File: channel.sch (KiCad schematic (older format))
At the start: 8 parts, among them Q1 MMBT5551, Q2 MMBT5401, Q3 NTMS4807, Q4 NTMS4807

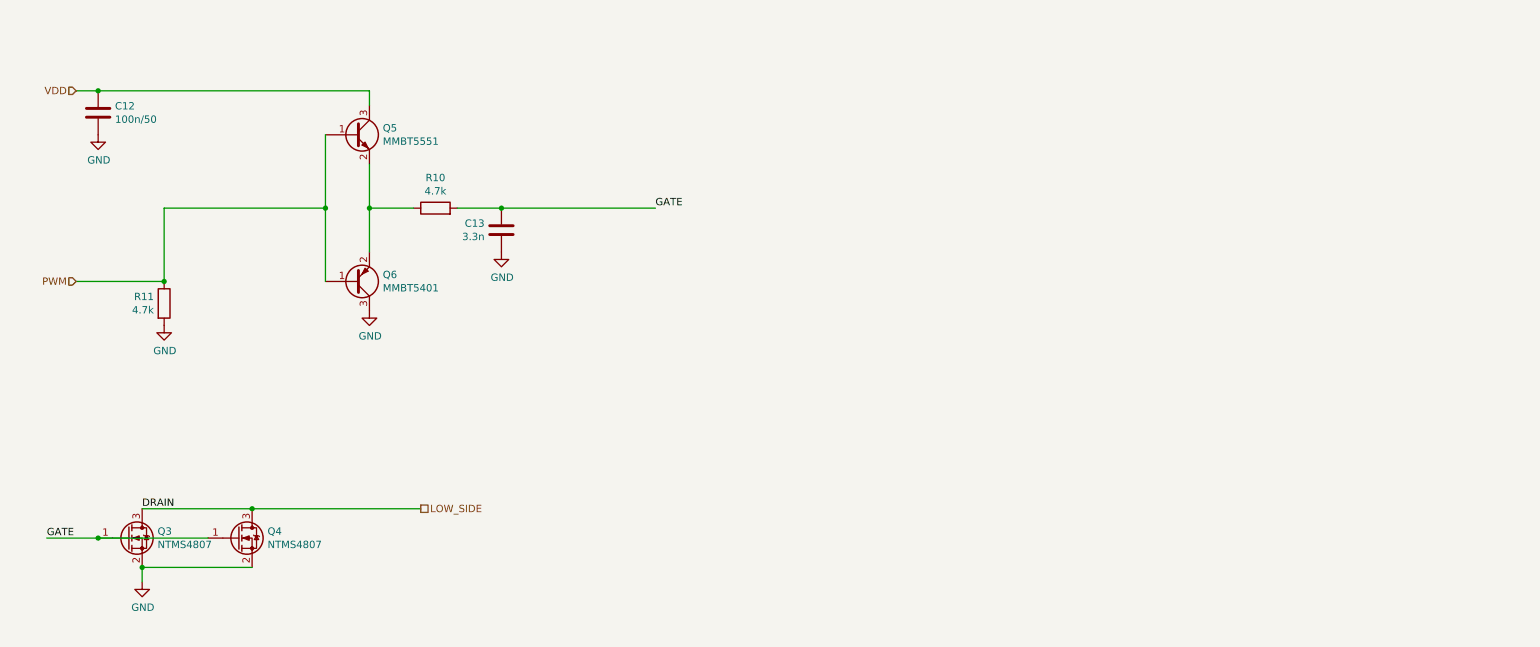
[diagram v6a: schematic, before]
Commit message: we can tolerate higher frequencies as long as our led strips are only a dozen or so metres long
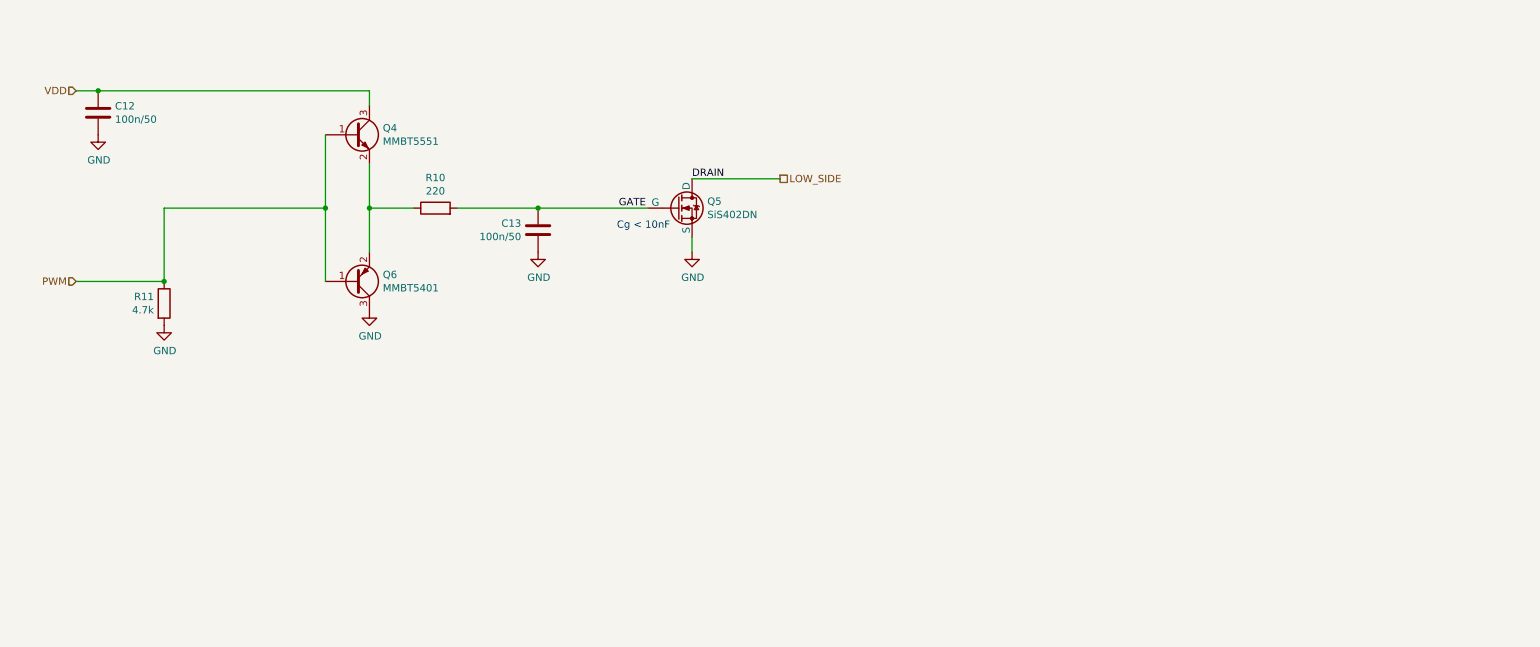
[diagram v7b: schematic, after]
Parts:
- removed Q3, Q4: NTMS4807, mark:NTMS-4807N-SOIC-8-3.9x4.9x1.27P, symbol Transistor_FET:AO3400A
- added Q2: SiS402DN, Package_SO:Vishay_PowerPAK_1212-8_Single, symbol mark:SiS402DN
- C11: value 3.3n -> 100n/50; JLC C26404 -> C307331
- R8: value 4.7k -> 220; JLC C25900 -> C25091
- renumbered Q2 to Q3
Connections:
- net GATE: now also Q2.4 (G)
- net GND: now also Q2.1 (S), Q2.2 (S), Q2.3 (S)
- net LOW_SIDE: now also Q2.5 (D)
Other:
- note added: "Cg < 10nF"
- moved on the sheet: C13
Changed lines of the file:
@@
 $Descr A4 11693 8268
 encoding utf-8
-Sheet 3 5
+Sheet 2 5
 Title ""
 Date ""
@@
 AR Path="/61C031A1/61C0AE1D" Ref="#PWR?"  Part="1"
 AR Path="/61C031A3/61C0AE1D" Ref="#PWR?"  Part="1"
-AR Path="/6202E846/61C0AE1D" Ref="#PWR027"  Part="1"
-AR Path="/620593AE/61C0AE1D" Ref="#PWR032"  Part="1"
-F 0 "#PWR032" H 3000 2400 50  0001 C CNN
+AR Path="/6202E846/61C0AE1D" Ref="#PWR030"  Part="1"
+AR Path="/620593AE/61C0AE1D" Ref="#PWR035"  Part="1"
+F 0 "#PWR035" H 3000 2400 50  0001 C CNN
 F 1 "GND" H 3005 2477 50  0000 C CNN
 F 2 "" H 3000 2650 50  0001 C CNN
@@
 AR Path="/61C031A1/61C1051F" Ref="#PWR?"  Part="1"
 AR Path="/61C031A3/61C1051F" Ref="#PWR?"  Part="1"
-AR Path="/6202E846/61C1051F" Ref="#PWR028"  Part="1"
-AR Path="/620593AE/61C1051F" Ref="#PWR033"  Part="1"
-F 0 "#PWR033" H 1600 2500 50  0001 C CNN
+AR Path="/6202E846/61C1051F" Ref="#PWR031"  Part="1"
+AR Path="/620593AE/61C1051F" Ref="#PWR036"  Part="1"
+F 0 "#PWR036" H 1600 2500 50  0001 C CNN
 F 1 "GND" H 1605 2577 50  0000 C CNN
 F 2 "" H 1600 2750 50  0001 C CNN
@@
 PWM
 $Comp
-L power:GND #PWR?
-U 1 1 61C20664
-P 3900 2250
-AR Path="/61C20664" Ref="#PWR?"  Part="1"
-AR Path="/61B5C5B6/61C20664" Ref="#PWR?"  Part="1"
-AR Path="/61C03040/61C20664" Ref="#PWR?"  Part="1"
-AR Path="/61C031A1/61C20664" Ref="#PWR?"  Part="1"
-AR Path="/61C031A3/61C20664" Ref="#PWR?"  Part="1"
-AR Path="/6202E846/61C20664" Ref="#PWR026"  Part="1"
-AR Path="/620593AE/61C20664" Ref="#PWR031"  Part="1"
-F 0 "#PWR031" H 3900 2000 50  0001 C CNN
-F 1 "GND" H 3905 2077 50  0000 C CNN
-F 2 "" H 3900 2250 50  0001 C CNN
-F 3 "" H 3900 2250 50  0001 C CNN
-	1    3900 2250
-	1    0    0    -1
-$EndComp
-$Comp
 L Transistor_BJT:MMBT5551L Q1
 U 1 1 61C0A1BB
 P 2900 1450
 AR Path="/6202E846/61C0A1BB" Ref="Q1"  Part="1"
-AR Path="/620593AE/61C0A1BB" Ref="Q5"  Part="1"
-F 0 "Q5" H 3091 1496 50  0000 L CNN
+AR Path="/620593AE/61C0A1BB" Ref="Q4"  Part="1"
+F 0 "Q4" H 3091 1496 50  0000 L CNN
 F 1 "MMBT5551" H 3091 1405 50  0000 L CNN
 F 2 "Package_TO_SOT_SMD:SOT-23" H 3100 1375 50  0001 L CIN
@@
 AR Path="/620593AE/61C5A1AF" Ref="R10"  Part="1"
 F 0 "R10" V 3657 1950 50  0000 C CNN
-F 1 "4.7k" V 3566 1950 50  0000 C CNN
+F 1 "220" V 3566 1950 50  0000 C CNN
 F 2 "Resistor_SMD:R_0402_1005Metric_Pad0.72x0.64mm_HandSolder" V 3380 1950 50  0001 C CNN
 F 3 "~" H 3450 1950 50  0001 C CNN
-F 4 "C25900" H 3450 1950 50  0001 C CNN "JLC"
+F 4 "C25091" H 3450 1950 50  0001 C CNN "JLC"
 	1    3450 1950
 	0    -1   -1   0
@@
 	3000 1150 3000 1250
 $Comp
-L Device:C C?
-U 1 1 61C61D09
-P 3900 2100
-AR Path="/61C61D09" Ref="C?"  Part="1"
-AR Path="/6202E846/61C61D09" Ref="C11"  Part="1"
-AR Path="/620593AE/61C61D09" Ref="C13"  Part="1"
-F 0 "C13" H 3785 2146 50  0000 R CNN
-F 1 "3.3n" H 3785 2055 50  0000 R CNN
-F 2 "Capacitor_SMD:C_0402_1005Metric_Pad0.74x0.62mm_HandSolder" H 3938 1950 50  0001 C CNN
-F 3 "~" H 3900 2100 50  0001 C CNN
-F 4 "C26404" H 3900 2100 50  0001 C CNN "JLC"
-	1    3900 2100
-	1    0    0    -1
-$EndComp
-$Comp
-L Device:Q_PNP_BEC Q2
+L Device:Q_PNP_BEC Q3
 U 1 1 61C4E023
 P 2900 2450
-AR Path="/6202E846/61C4E023" Ref="Q2"  Part="1"
+AR Path="/6202E846/61C4E023" Ref="Q3"  Part="1"
 AR Path="/620593AE/61C4E023" Ref="Q6"  Part="1"
 F 0 "Q6" H 3091 2404 50  0000 L CNN
@@
 	1    0    0    1
 $EndComp
-Wire Wire Line
-	3600 1950 3900 1950
-Connection ~ 3900 1950
 Wire Wire Line
 	3000 2250 3000 1950
@@
 AR Path="/61C031A1/61D15BBF" Ref="#PWR?"  Part="1"
 AR Path="/61C031A3/61D15BBF" Ref="#PWR?"  Part="1"
-AR Path="/6202E846/61D15BBF" Ref="#PWR025"  Part="1"
-AR Path="/620593AE/61D15BBF" Ref="#PWR030"  Part="1"
-F 0 "#PWR030" H 1150 1200 50  0001 C CNN
+AR Path="/6202E846/61D15BBF" Ref="#PWR027"  Part="1"
+AR Path="/620593AE/61D15BBF" Ref="#PWR032"  Part="1"
+F 0 "#PWR032" H 1150 1200 50  0001 C CNN
 F 1 "GND" H 1155 1277 50  0000 C CNN
 F 2 "" H 1150 1450 50  0001 C CNN
@@
 Wire Wire Line
 	2700 1950 2700 2450
-Wire Wire Line
-	3900 1950 4950 1950
-Text Label 4950 1950 0    50   ~ 0
-GATE
-Text HLabel 3350 4000 2    50   UnSpc ~ 0
+Text Notes 5050 2100 2    50   ~ 0
+Cg < 10nF
+Wire Wire Line
+	4150 1950 4900 1950
+Wire Wire Line
+	5200 1750 5800 1750
+$Comp
+L mark:SiS402DN Q2
+U 1 1 622D62B8
+P 5100 1950
+AR Path="/6202E846/622D62B8" Ref="Q2"  Part="1"
+AR Path="/620593AE/622D62B8" Ref="Q5"  Part="1"
+F 0 "Q5" H 5304 1996 50  0000 L CNN
+F 1 "SiS402DN" H 5304 1905 50  0000 L CNN
+F 2 "Package_SO:Vishay_PowerPAK_1212-8_Single" H 5100 2450 50  0001 C CNN
+F 3 "https://datasheet.lcsc.com/lcsc/1809301517_Vishay-Intertech-SIS402DN-T1-GE3_C15791.pdf" H 5100 1950 50  0001 C CNN
+	1    5100 1950
+	1    0    0    -1
+$EndComp
+Text HLabel 5800 1750 2    50   UnSpc ~ 0
 LOW_SIDE
 $Comp
 L power:GND #PWR?
 U 1 1 6203BB32
-P 1450 4500
+P 5200 2250
 AR Path="/61B5C5B6/6203BB32" Ref="#PWR?"  Part="1"
 AR Path="/61C03040/6203BB32" Ref="#PWR?"  Part="1"
@@
 AR Path="/6202E846/6203BB32" Ref="#PWR029"  Part="1"
 AR Path="/620593AE/6203BB32" Ref="#PWR034"  Part="1"
-F 0 "#PWR029" H 1450 4250 50  0001 C CNN
-F 1 "GND" H 1455 4327 50  0000 C CNN
-F 2 "" H 1450 4500 50  0001 C CNN
-F 3 "" H 1450 4500 50  0001 C CNN
-	1    1450 4500
-	1    0    0    -1
-$EndComp
-Text Label 1450 4000 0    50   ~ 0
+F 0 "#PWR034" H 5200 2000 50  0001 C CNN
+F 1 "GND" H 5205 2077 50  0000 C CNN
+F 2 "" H 5200 2250 50  0001 C CNN
+F 3 "" H 5200 2250 50  0001 C CNN
+	1    5200 2250
+	1    0    0    -1
+$EndComp
+Text Label 5200 1750 0    50   ~ 0
 DRAIN
-Text Label 800  4200 0    50   ~ 0
+Text Label 4700 1950 0    50   ~ 0
 GATE
 Wire Wire Line
-	1450 4500 1450 4400
-Wire Wire Line
-	1450 4400 2200 4400
-Wire Wire Line
-	2200 4000 3350 4000
-Wire Wire Line
-	2200 4000 1450 4000
-Connection ~ 2200 4000
-$Comp
-L Transistor_FET:AO3400A Q?
-U 1 1 6203BAE5
-P 2100 4200
-AR Path="/61B5C5B6/6203BAE5" Ref="Q?"  Part="1"
-AR Path="/61C03040/6203BAE5" Ref="Q?"  Part="1"
-AR Path="/61C031A1/6203BAE5" Ref="Q?"  Part="1"
-AR Path="/61C031A3/6203BAE5" Ref="Q?"  Part="1"
-AR Path="/6203BAE5" Ref="Q?"  Part="1"
-AR Path="/6202E846/6203BAE5" Ref="Q4"  Part="1"
-AR Path="/620593AE/6203BAE5" Ref="Q8"  Part="1"
-F 0 "Q4" H 2305 4246 50  0000 L CNN
-F 1 "NTMS4807" H 2305 4155 50  0000 L CNN
-F 2 "mark:NTMS-4807N-SOIC-8-3.9x4.9x1.27P" H 2300 4125 50  0001 L CIN
-F 3 "https://datasheet.lcsc.com/lcsc/1809171608_ON-Semiconductor-NTMS4807NR2G_C80851.pdf" H 2100 4200 50  0001 L CNN
-F 4 "C80851" H 2100 4200 50  0001 C CNN "JLC"
-	1    2100 4200
-	1    0    0    -1
-$EndComp
-Connection ~ 1450 4400
-Wire Wire Line
-	800  4200 1150 4200
-Wire Wire Line
-	1150 4200 1900 4200
-Connection ~ 1150 4200
-$Comp
-L Transistor_FET:AO3400A Q?
-U 1 1 6203BADE
-P 1350 4200
-AR Path="/61B5C5B6/6203BADE" Ref="Q?"  Part="1"
-AR Path="/61C03040/6203BADE" Ref="Q?"  Part="1"
-AR Path="/61C031A1/6203BADE" Ref="Q?"  Part="1"
-AR Path="/61C031A3/6203BADE" Ref="Q?"  Part="1"
-AR Path="/6203BADE" Ref="Q?"  Part="1"
-AR Path="/6202E846/6203BADE" Ref="Q3"  Part="1"
-AR Path="/620593AE/6203BADE" Ref="Q7"  Part="1"
-F 0 "Q3" H 1555 4246 50  0000 L CNN
-F 1 "NTMS4807" H 1555 4155 50  0000 L CNN
-F 2 "mark:NTMS-4807N-SOIC-8-3.9x4.9x1.27P" H 1550 4125 50  0001 L CIN
-F 3 "https://datasheet.lcsc.com/lcsc/1809171608_ON-Semiconductor-NTMS4807NR2G_C80851.pdf" H 1350 4200 50  0001 L CNN
-F 4 "C80851" H 1350 4200 50  0001 C CNN "JLC"
-	1    1350 4200
-	1    0    0    -1
-$EndComp
+	5200 2250 5200 2150
+Connection ~ 4150 1950
+Wire Wire Line
+	3600 1950 4150 1950
+$Comp
+L Device:C C?
+U 1 1 61C61D09
+P 4150 2100
+AR Path="/61C61D09" Ref="C?"  Part="1"
+AR Path="/6202E846/61C61D09" Ref="C11"  Part="1"
+AR Path="/620593AE/61C61D09" Ref="C13"  Part="1"
+F 0 "C13" H 4035 2146 50  0000 R CNN
+F 1 "100n/50" H 4035 2055 50  0000 R CNN
+F 2 "Capacitor_SMD:C_0402_1005Metric_Pad0.74x0.62mm_HandSolder" H 4188 1950 50  0001 C CNN
+F 3 "~" H 4150 2100 50  0001 C CNN
+F 4 "C307331" H 4150 2100 50  0001 C CNN "JLC"
+	1    4150 2100
+	1    0    0    -1
+$EndComp
+$Comp
+L power:GND #PWR?
+U 1 1 61C20664
+P 4150 2250
+AR Path="/61C20664" Ref="#PWR?"  Part="1"
+AR Path="/61B5C5B6/61C20664" Ref="#PWR?"  Part="1"
+AR Path="/61C03040/61C20664" Ref="#PWR?"  Part="1"
+AR Path="/61C031A1/61C20664" Ref="#PWR?"  Part="1"
+AR Path="/61C031A3/61C20664" Ref="#PWR?"  Part="1"
+AR Path="/6202E846/61C20664" Ref="#PWR028"  Part="1"
+AR Path="/620593AE/61C20664" Ref="#PWR033"  Part="1"
+F 0 "#PWR033" H 4150 2000 50  0001 C CNN
+F 1 "GND" H 4155 2077 50  0000 C CNN
+F 2 "" H 4150 2250 50  0001 C CNN
+F 3 "" H 4150 2250 50  0001 C CNN
+	1    4150 2250
+	1    0    0    -1
+$EndComp
